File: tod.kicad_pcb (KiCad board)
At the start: 2 copper layers, 72 x 57 mm, 67 parts, among them J1 Conn_01x04, J2 Conn_01x03, J3 Conn_01x04, J4 Conn_01x03, Q1 BC856B, Q2 BC817, Q3 BC856B, Q4 BC817, Q5 BC856, Q6 BC817, Q7 BC856, Q8 BC817, U1 PC817, U2 PC817, U3 PC817, U4 PC817

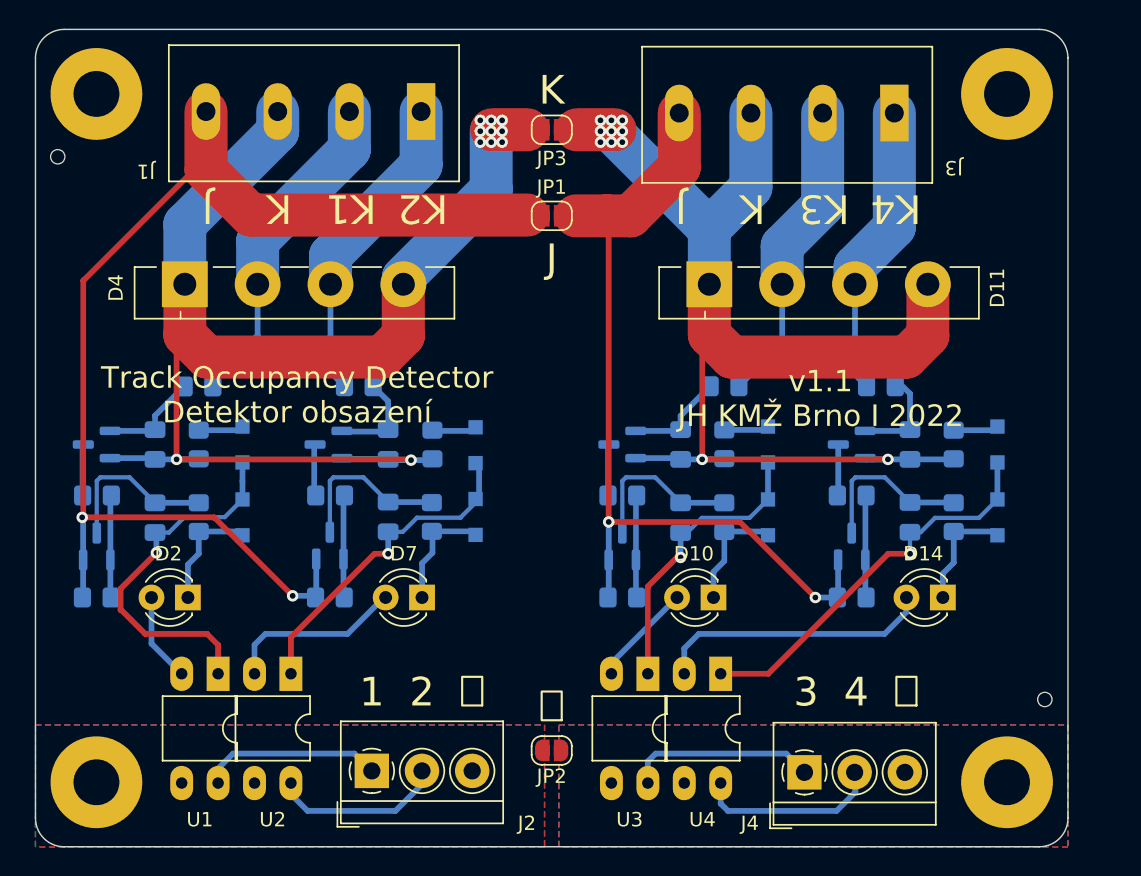
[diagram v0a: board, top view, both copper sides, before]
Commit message: Add heatplanes.
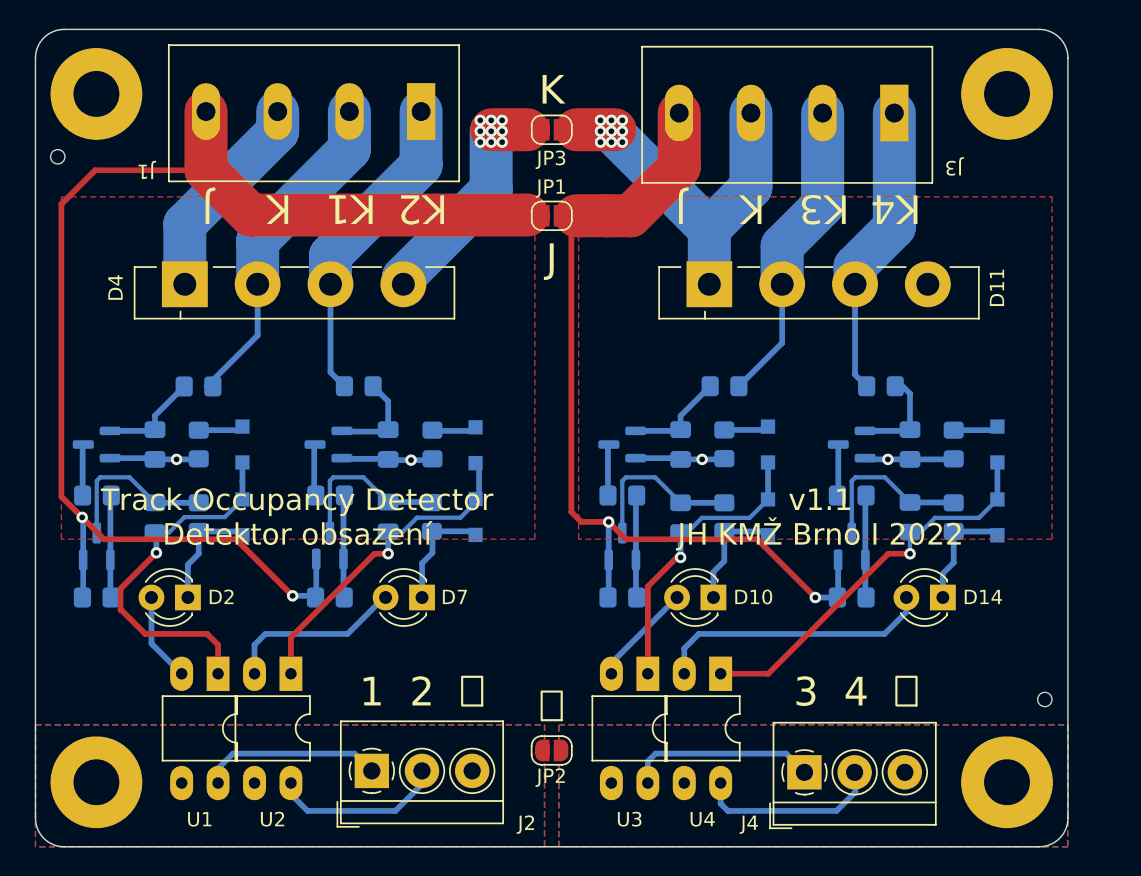
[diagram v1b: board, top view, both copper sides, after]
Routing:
- net /K2: track 89.2 -> 37.9 mm
- net /K1: track 92.0 -> 43.1 mm
- net /J1: track 85.7 -> 88.2 mm
- net /J2: track 59.8 -> 61.3 mm
- added copper zone on F.Cu, net /K1
- added copper zone on F.Cu, net /K2
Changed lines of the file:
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@@
     (property "Sheetname" "")
     (attr through_hole)
-    (fp_text reference "D7" (at 1.275 3.048) (layer "F.SilkS")
+    (fp_text reference "D7" (at -2.281 0) (layer "F.SilkS")
       (effects (font (size 1 1) (thickness 0.15)))
     )
@@
     (property "Sheetname" "")
     (attr through_hole)
-    (fp_text reference "D10" (at 1.366487 3.048) (layer "F.SilkS")
+    (fp_text reference "D10" (at -2.789 0) (layer "F.SilkS")
       (effects (font (size 1 1) (thickness 0.15)))
     )
@@
     (property "Sheetname" "")
     (attr through_hole)
-    (fp_text reference "D14" (at 1.366487 3.048) (layer "F.SilkS")
+    (fp_text reference "D14" (at -2.794 0) (layer "F.SilkS")
       (effects (font (size 1 1) (thickness 0.15)))
     )
@@
     (property "Sheetname" "")
     (attr through_hole)
-    (fp_text reference "D2" (at 1.366487 3.048) (layer "F.SilkS")
+    (fp_text reference "D2" (at -2.355 0) (layer "F.SilkS")
       (effects (font (size 1 1) (thickness 0.15)))
     )
@@
     (effects (font (size 2 2) (thickness 0.15)))
   )
-  (gr_text "v1.1\nJH KMŽ Brno I 2022" (at 167.75 88.75) (layer "F.SilkS")
+  (gr_text "v1.1\nJH KMŽ Brno I 2022" (at 167.75 97.028) (layer "F.SilkS")
     (effects (font (size 1.5 1.5) (thickness 0.15)))
   )
@@
     (effects (font (size 2 2) (thickness 0.15)) (justify mirror))
   )
-  (gr_text "Track Occupancy Detector\nDetektor obsazení" (at 131.25 88.5) (layer "F.SilkS")
+  (gr_text "Track Occupancy Detector\nDetektor obsazení" (at 131.25 97.028) (layer "F.SilkS")
     (effects (font (size 1.5 1.5) (thickness 0.15)))
   )
@@
     (effects (font (size 2 2) (thickness 0.15)) (justify mirror))
   )
-  (segment (start 122.8405 92.9855) (end 122.8405 84.8715) (width 0.4) (layer "F.Cu") (net 1))
-  (segment (start 137.16 85.852) (end 124.968 85.852) (width 3) (layer "F.Cu") (net 1))
-  (segment (start 123.414 84.298) (end 123.414 80.772) (width 3) (layer "F.Cu") (net 1))
   (segment (start 139.1395 92.9855) (end 139.1915 93.0375) (width 0.4) (layer "F.Cu") (net 1))
-  (segment (start 138.654 80.772) (end 138.654 84.358) (width 3) (layer "F.Cu") (net 1))
   (segment (start 122.8405 92.9855) (end 122.862 92.964) (width 0.4) (layer "F.Cu") (net 1))
-  (segment (start 138.654 84.358) (end 137.16 85.852) (width 3) (layer "F.Cu") (net 1))
-  (segment (start 124.968 85.852) (end 123.414 84.298) (width 3) (layer "F.Cu") (net 1))
-  (segment (start 122.8405 92.9855) (end 139.1395 92.9855) (width 0.4) (layer "F.Cu") (net 1))
   (segment (start 144.82 70) (end 147.32 70) (width 3) (layer "F.Cu") (net 1))
-  (segment (start 122.8405 84.8715) (end 123.414 84.298) (width 0.4) (layer "F.Cu") (net 1))
   (via (at 122.8405 92.9855) (size 0.8) (drill 0.4) (layers "F.Cu" "B.Cu") (net 1))
   (via (at 145.542 70.866) (size 0.8) (drill 0.4) (layers "F.Cu" "B.Cu") (net 1))
@@
   (segment (start 137.434 95.9625) (end 140.6465 95.9625) (width 0.4) (layer "B.Cu") (net 7))
   (segment (start 133.53 98.0625) (end 133.53 94.488) (width 0.3) (layer "B.Cu") (net 7))
-  (segment (start 175.23 80.772) (end 175.23 84.358) (width 3) (layer "F.Cu") (net 8))
-  (segment (start 175.23 84.358) (end 173.736 85.852) (width 3) (layer "F.Cu") (net 8))
-  (segment (start 159.4165 81.3455) (end 159.99 80.772) (width 0.4) (layer "F.Cu") (net 8))
-  (segment (start 161.544 85.852) (end 159.99 84.298) (width 3) (layer "F.Cu") (net 8))
-  (segment (start 159.99 84.298) (end 159.99 80.772) (width 3) (layer "F.Cu") (net 8))
-  (segment (start 159.4905 92.9855) (end 172.4445 92.9855) (width 0.4) (layer "F.Cu") (net 8))
-  (segment (start 159.4905 81.2715) (end 159.99 80.772) (width 0.4) (layer "F.Cu") (net 8))
-  (segment (start 173.736 85.852) (end 161.544 85.852) (width 3) (layer "F.Cu") (net 8))
-  (segment (start 159.4905 92.9855) (end 159.4905 81.2715) (width 0.4) (layer "F.Cu") (net 8))
   (segment (start 153.416 70) (end 150.75 70) (width 3) (layer "F.Cu") (net 8))
-  (segment (start 159.4165 84.8715) (end 159.99 84.298) (width 0.4) (layer "F.Cu") (net 8))
-  (segment (start 159.512 81.25) (end 159.99 80.772) (width 0.4) (layer "F.Cu") (net 8))
   (via (at 159.4905 92.9855) (size 0.8) (drill 0.4) (layers "F.Cu" "B.Cu") (net 8))
   (via (at 152.4 70.104) (size 0.8) (drill 0.4) (layers "F.Cu" "B.Cu") (net 8))
@@
   (segment (start 172.212 105.156) (end 159.258 105.156) (width 0.4) (layer "B.Cu") (net 30))
   (segment (start 173.736 102.616) (end 173.736 103.632) (width 0.4) (layer "B.Cu") (net 30))
-  (segment (start 116.332 80.518) (end 116.332 96.954) (width 0.4) (layer "F.Cu") (net 31))
-  (segment (start 125.462 97.028) (end 130.934 102.5) (width 0.4) (layer "F.Cu") (net 31))
-  (segment (start 116.332 96.954) (end 116.258 97.028) (width 0.4) (layer "F.Cu") (net 31))
+  (segment (start 116.258 97.028) (end 114.808 95.578) (width 0.4) (layer "F.Cu") (net 31))
+  (segment (start 117.782 98.552) (end 126.986 98.552) (width 0.4) (layer "F.Cu") (net 31))
+  (segment (start 126.986 98.552) (end 130.934 102.5) (width 0.4) (layer "F.Cu") (net 31))
+  (segment (start 114.808 95.578) (end 114.808 75.184) (width 0.4) (layer "F.Cu") (net 31))
+  (segment (start 117.17 72.822) (end 124.892 72.822) (width 0.4) (layer "F.Cu") (net 31))
+  (segment (start 114.808 75.184) (end 117.17 72.822) (width 0.4) (layer "F.Cu") (net 31))
   (segment (start 128.016 75.946) (end 147.32 75.946) (width 3) (layer "F.Cu") (net 31))
   (segment (start 124.892 72.822) (end 124.892 68.728) (width 3) (layer "F.Cu") (net 31))
-  (segment (start 123.824 73.026) (end 116.332 80.518) (width 0.4) (layer "F.Cu") (net 31))
   (segment (start 128.016 75.946) (end 124.892 72.822) (width 3) (layer "F.Cu") (net 31))
-  (segment (start 123.824 69) (end 123.824 73.026) (width 0.4) (layer "F.Cu") (net 31))
-  (segment (start 116.258 97.028) (end 125.462 97.028) (width 0.4) (layer "F.Cu") (net 31))
+  (segment (start 116.258 97.028) (end 117.782 98.552) (width 0.4) (layer "F.Cu") (net 31))
+  (segment (start 123.824 69) (end 123.824 69.216) (width 0.4) (layer "F.Cu") (net 31))
   (via (at 116.258 97.028) (size 0.8) (drill 0.4) (layers "F.Cu" "B.Cu") (net 31))
   (via (at 130.934 102.5) (size 0.8) (drill 0.4) (layers "F.Cu" "B.Cu") (net 31))
@@
   (segment (start 138.101 117.5) (end 131.978 117.5) (width 0.4) (layer "B.Cu") (net 33))
   (segment (start 128.275 115.555) (end 128.275 115.775) (width 0.4) (layer "B.Cu") (net 34))
-  (segment (start 152.974 76.12) (end 152.854 76) (width 0.4) (layer "F.Cu") (net 35))
+  (segment (start 151.069 97.348) (end 150.368 96.647) (width 0.4) (layer "F.Cu") (net 35))
   (segment (start 157.892 68.834) (end 157.892 72.608) (width 3) (layer "F.Cu") (net 35))
-  (segment (start 162.118 97.348) (end 152.974 97.348) (width 0.4) (layer "F.Cu") (net 35))
-  (segment (start 152.974 97.348) (end 152.974 76.12) (width 0.4) (layer "F.Cu") (net 35))
+  (segment (start 163.322 98.552) (end 154.178 98.552) (width 0.4) (layer "F.Cu") (net 35))
+  (segment (start 152.974 97.348) (end 151.069 97.348) (width 0.4) (layer "F.Cu") (net 35))
+  (segment (start 150.368 96.647) (end 150.368 76.708) (width 0.4) (layer "F.Cu") (net 35))
   (segment (start 152.854 76) (end 150.7 76) (width 3) (layer "F.Cu") (net 35))
-  (segment (start 167.386 102.616) (end 162.118 97.348) (width 0.4) (layer "F.Cu") (net 35))
+  (segment (start 154.178 98.552) (end 152.974 97.348) (width 0.4) (layer "F.Cu") (net 35))
+  (segment (start 167.386 102.616) (end 163.322 98.552) (width 0.4) (layer "F.Cu") (net 35))
   (segment (start 154.5 76) (end 152.854 76) (width 3) (layer "F.Cu") (net 35))
   (segment (start 157.892 72.608) (end 154.5 76) (width 3) (layer "F.Cu") (net 35))
@@
       )
     )
+  )
+  (zone (net 8) (net_name "/K2") (layer "F.Cu") (hatch edge 0.508)
+    (connect_pads (clearance 0.508))
+    (min_thickness 0.254) (filled_areas_thickness no)
+    (fill yes (thermal_gap 0.508) (thermal_bridge_width 0.508))
+    (polygon
+      (pts
+        (xy 183.896 98.552)
+        (xy 150.876 98.552)
+        (xy 150.876 74.676)
+        (xy 183.896 74.676)
+      )
+    )
+  )
+  (zone (net 1) (net_name "/K1") (layer "F.Cu") (hatch edge 0.508)
+    (connect_pads (clearance 0.508))
+    (min_thickness 0.254) (filled_areas_thickness no)
+    (fill yes (thermal_gap 0.508) (thermal_bridge_width 0.508))
+    (polygon
+      (pts
+        (xy 147.828 98.552)
+        (xy 114.808 98.552)
+        (xy 114.808 74.676)
+        (xy 147.828 74.676)
+      )
+    )

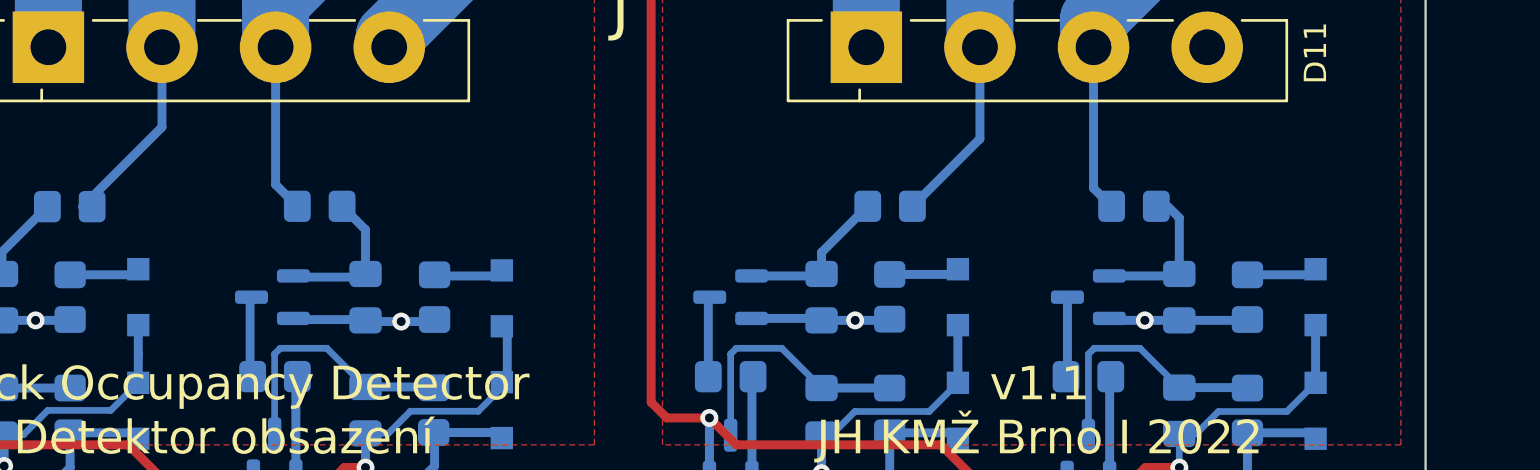
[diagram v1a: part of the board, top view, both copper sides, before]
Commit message: Add silkscreen texts & logos.
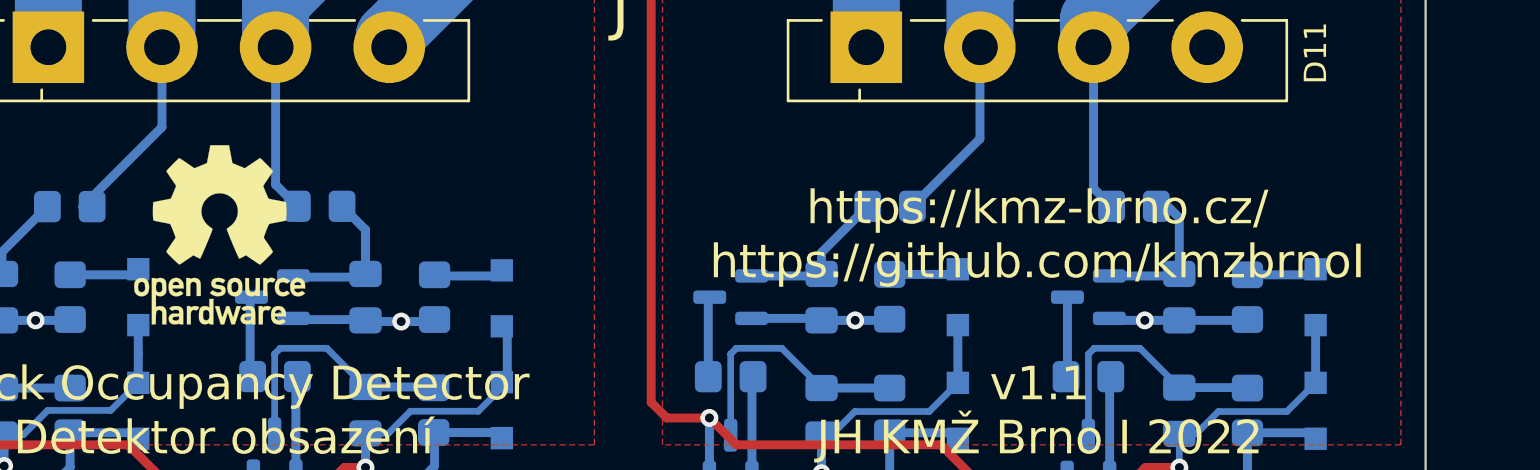
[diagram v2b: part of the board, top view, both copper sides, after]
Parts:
- added REF**: OSHW-Logo_7.5x8mm_SilkScreen, Symbol:OSHW-Logo_7.5x8mm_SilkScreen, F.Cu at (131.1, 89.2)
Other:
- board text added: "https://kmz-brno.cz/ https://github.com/kmzbrnoI"

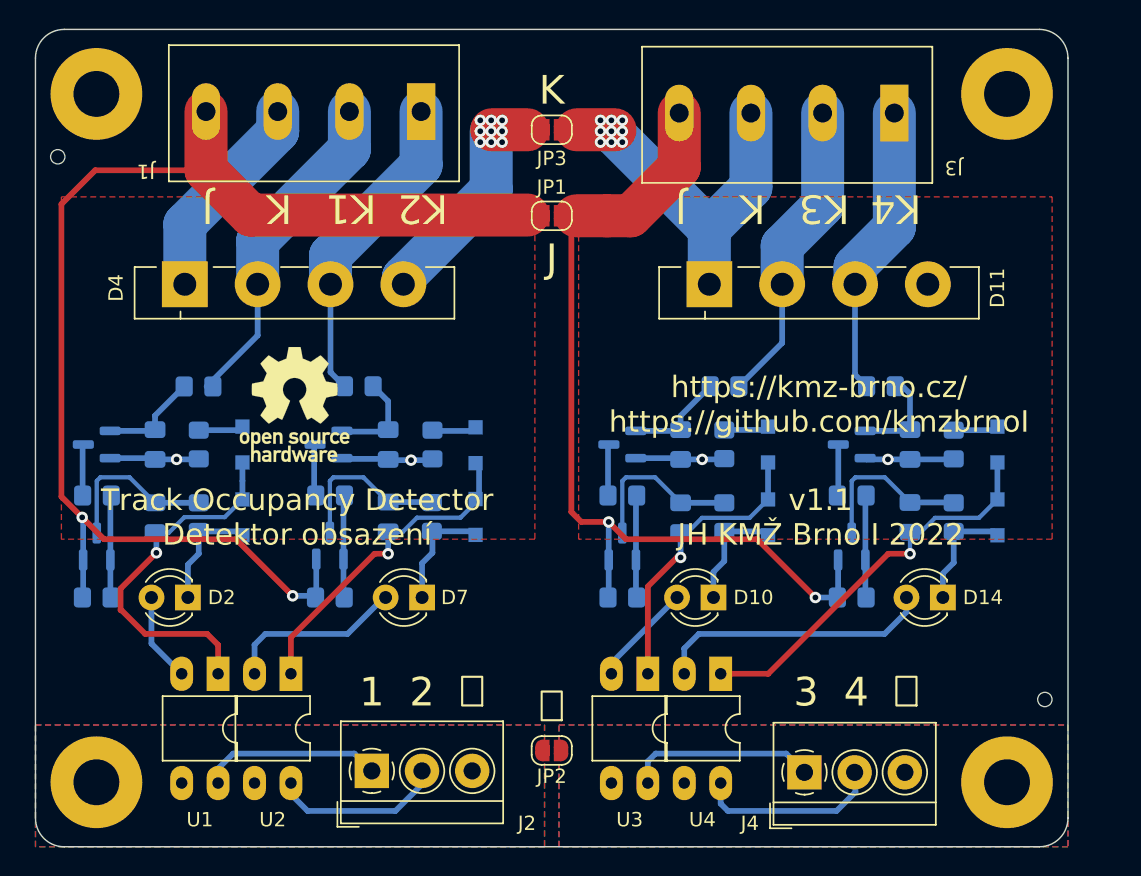
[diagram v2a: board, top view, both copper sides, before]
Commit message: Add JLCJLCJLCJLC text for manufacturing id.
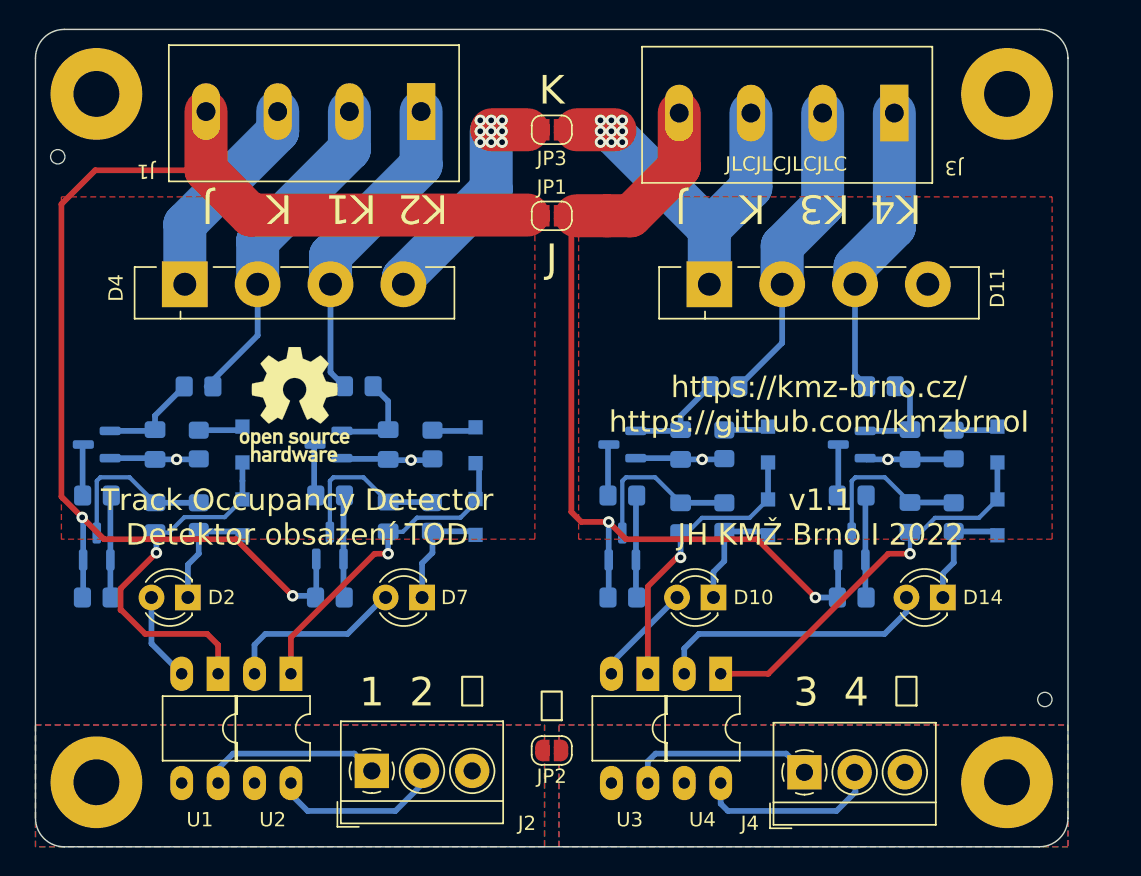
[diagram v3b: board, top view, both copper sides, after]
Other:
- board text added: "JLCJLCJLCJLC"
- board text added: "Track Occupancy Detector Detektor obsazení TOD"
- board text removed: "Track Occupancy Detector Detektor obsazení"
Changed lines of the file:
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@@
     (effects (font (size 1.5 1.5) (thickness 0.15)))
   )
-  (gr_text "Track Occupancy Detector\nDetektor obsazení" (at 131.25 97.028) (layer "F.SilkS")
+  (gr_text "Track Occupancy Detector\nDetektor obsazení TOD" (at 131.25 97.028) (layer "F.SilkS")
     (effects (font (size 1.5 1.5) (thickness 0.15)))
   )
@@
     (effects (font (size 2 2) (thickness 0.15)) (justify mirror))
   )
+  (gr_text "JLCJLCJLCJLC" (at 165.354 72.39) (layer "F.SilkS")
+    (effects (font (size 1 1) (thickness 0.15)))
+  )
   (segment (start 139.1395 92.9855) (end 139.1915 93.0375) (width 0.4) (layer "F.Cu") (net 1))
